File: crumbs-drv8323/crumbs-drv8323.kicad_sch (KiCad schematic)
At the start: 22 parts, among them J1 MotorConn, J2 Conn_02x05_Odd_Even, J3 Conn_02x05_Odd_Even, J4 Conn_01x02, Q1 Q_NMOS, Q2 Q_NMOS, Q3 Q_NMOS, Q4 Q_NMOS, Q5 Q_NMOS, Q6 Q_NMOS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

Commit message: feat: first iteration on drv8323 schematic
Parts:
- added C7: 100nF / 16V, Capacitor_SMD:C_0805_2012Metric, symbol Device:C
- added C8: 47uF / 16V, Capacitor_SMD:C_0805_2012Metric, symbol Device:C
- added C9: 4.7uF / VM, symbol Device:C_Polarized
- added D1: 1N5819, Diode_THT:D_DO-41_SOD81_P10.16mm_Horizontal, symbol Diode:1N5819
- added J3: VCC_to_3.3V, Connector_PinHeader_2.54mm:PinHeader_1x03_P2.54mm_Vertical, symbol Connector_Generic:Conn_01x03
- added J6: Conn_01x03, Connector_PinHeader_2.54mm:PinHeader_1x03_P2.54mm_Vertical, symbol Connector_Generic:Conn_01x03
- added L1: 22uH / 2A, symbol Device:L
- added R6: 4K7, Resistor_SMD:R_0805_2012Metric, symbol Device:R_US
- added RFBB1: 30K, Resistor_SMD:R_0805_2012Metric, symbol Device:R_US
- added RFBT1: 100K, Resistor_SMD:R_0805_2012Metric, symbol Device:R_US
- added RT1: 34K8, Resistor_SMD:R_0805_2012Metric, symbol Device:R_US
- added U2: LMR16010PDDAR, easyeda2kicad:SOPOWERPAD-8_L4.9-W3.9-P1.27-LS6.0-BL-EP, symbol easyeda2kicad:LMR16010PDDAR
- C1: renamed from C3; value C -> 22uF
- C2: value C -> 100nF
- C3: renamed from C1; value C -> 1uF/16V
- C4: value C -> 47nF
- C5: renamed from C6; value C -> 1uF/6.3V
- C6: renamed from C5; value C -> 100nF
- R1: renamed from R4; value ~ -> 4K7
- R2: renamed from R5; value ~ -> 4K7
- R3: value RSense -> 2m
- R4: renamed from R2; value RSense -> 2m
- R5: renamed from R1; value RSense -> 2m
- U1: footprint DRV8323SRTAT:QFN50P600X600X80-41N415X415 -> symbols:QFN50P600X600X80-41N415X415
- renumbered J3 to J2, J2 to J5, Q5 to Q1, Q6 to Q2, Q1 to Q5, Q2 to Q6
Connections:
- net GND: now also J5.10 (Pin_10), U1.41 (EXP), C8.1, C9.2, D1.2 (A), RFBB1.2, RT1.2, U2.7 (GND), U2.9 (EP); no longer J5.8 (Pin_8)
- net VCC: now also J3.2 (Pin_2)
- net VM: now also J5.6 (Pin_6), C9.1, U2.2 (VIN), U2.3 (EN)
- new net: RFBB1.1, RFBT1.2, U2.5 (FB)
- new net: RT1.1, U2.4 (RT/SYNC)
- new net: C7.1, U2.1 (BOOT)
- new net: C7.2, D1.1 (K), L1.1, U2.8 (SW)
- new net +3V3: C8.2, J3.1 (Pin_1), J5.8 (Pin_8), L1.2, R6.1, RFBT1.1
- new net PGOOD: R6.2, U2.6 (PGOOD)
- no-connect marks 1 -> 0
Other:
- note added: "3.3-V internal regulator output This regulator can source up to 30 mA externally"
- note added: "65V Max"
- note added: "7V to 60V"
- note added: "ALL Capacitor Must be Higher than VM"
- note added: "About 700Khz"
- note added: "R_{FBT} = ((Vout - 0.75) / 0.75) x R_{FBB} 100K = ((3.3 - 0.75) / 0.75) x R_{FBB} R_{FBB} = 29500 ohm"
- note added: "R_{T}(KOhm) = 42904 x f_{sw}(Khz) For 700 KHz, the calculated RT is 34.44 kΩ and standard value 34.8 kΩ can be used to set the switching frequency at 700 KHz"
- note added: "Thermal Pad Must be connected to ground"
- note added: "VIL Input logic low voltage 0 - 0.8 V VIH Input logic high voltage 1.5 - 5.5 V"
- note added: "VM + 13.5V"
- note added: "VREF Reference voltage input (VREF) 3 - 5.5 V"
- moved on the sheet: C1, C2, C3, C4, C5, C6, J1, J2, J4, J5, Q1, Q2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

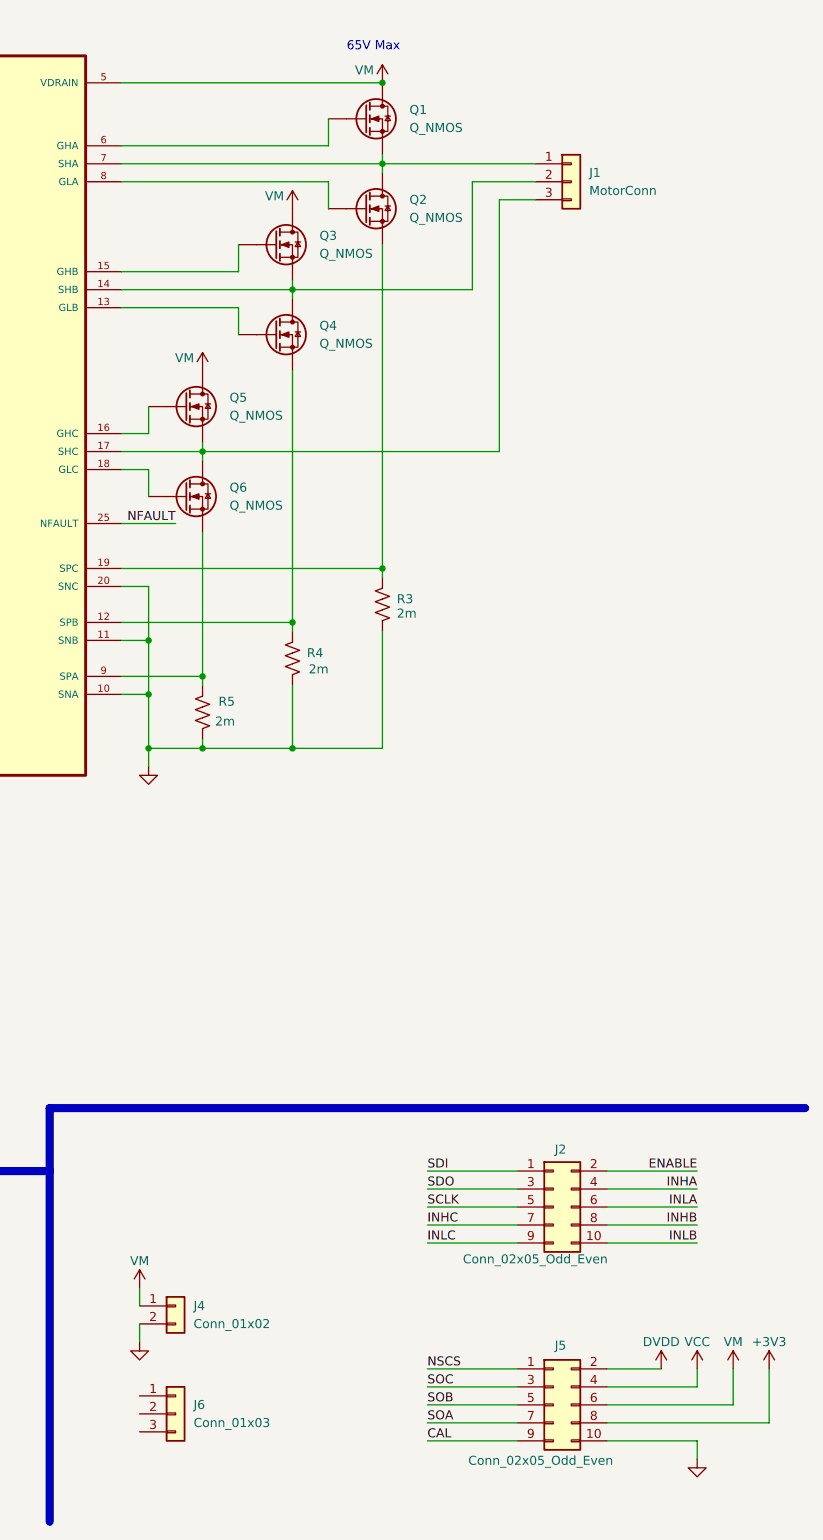
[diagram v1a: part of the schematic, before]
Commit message: feat: assign correct footprint
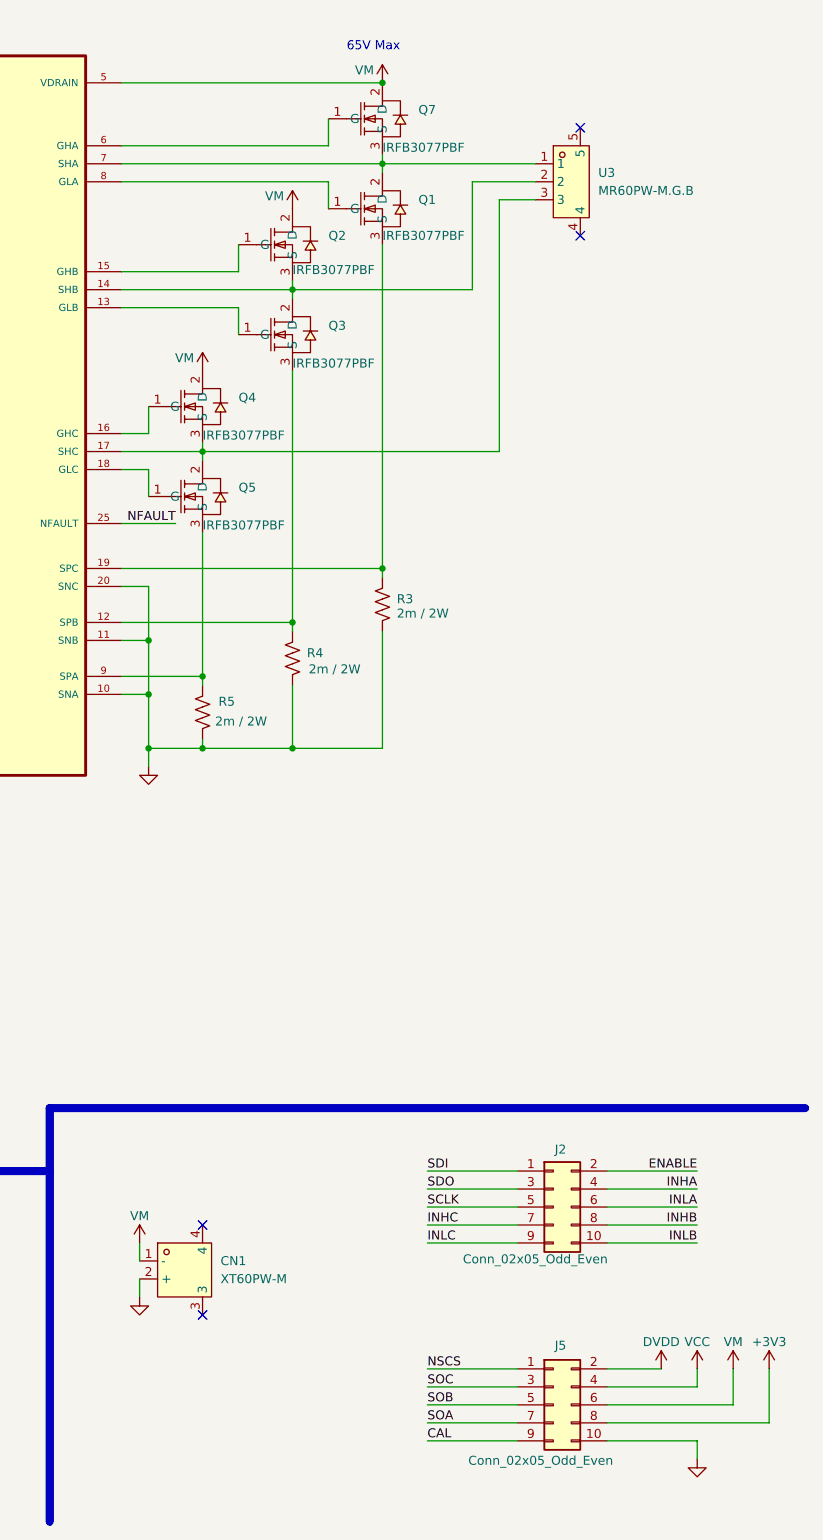
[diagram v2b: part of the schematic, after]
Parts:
- removed J1: MotorConn, symbol Connector_Generic:Conn_01x03
- removed J4: Conn_01x02, symbol Connector_Generic:Conn_01x02
- removed J6: Conn_01x03, Connector_PinHeader_2.54mm:PinHeader_1x03_P2.54mm_Vertical, symbol Connector_Generic:Conn_01x03
- removed Q1, Q2, Q3, Q4, Q5, Q6: Q_NMOS, symbol Device:Q_NMOS
- added CN1: XT60PW-M, easyeda2kicad:CONN-TH_XT60PW-M, symbol easyeda2kicad:XT60PW-M
- added Q1, Q2, Q3, Q4, Q5, Q7: IRFB3077PBF, easyeda2kicad:TO-220-3_L10.0-W4.5-P2.54-L, symbol easyeda2kicad:IRFB3077PBF
- added U3: MR60PW-M.G.B, easyeda2kicad:CONN-TH_MR60PW, symbol easyeda2kicad:MR60PW-M.G.B
- C1, C2, C4, C8: footprint Capacitor_SMD:C_0805_2012Metric -> Capacitor_THT:C_Disc_D7.5mm_W5.0mm_P5.00mm
- C9: footprint (none) -> Capacitor_THT:CP_Radial_D8.0mm_P2.50mm
- L1: footprint (none) -> Inductor_SMD:L_1812_4532Metric
- R3, R4, R5: value 2m -> 2m / 2W; footprint Resistor_SMD:R_0805_2012Metric -> Resistor_SMD:R_2512_6332Metric
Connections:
- net GND: now also CN1.2 (+)
- net VM: now also CN1.1 (-), Q2.2 (D), Q4.2 (D), Q7.2 (D)
- net at R4.1, U1.12 (SPB): now also Q3.3 (S)
- net at U1.13 (GLB): now also Q3.1 (G)
- net at U1.14 (SHB): now also Q2.3 (S), Q3.2 (D), U3.2
- net at U1.15 (GHB): now also Q2.1 (G)
- net at U1.16 (GHC): now also Q4.1 (G)
- net at U1.17 (SHC): now also Q4.3 (S), Q5.2 (D), U3.3
- net at U1.18 (GLC): now also Q5.1 (G)
- net at R3.1, U1.19 (SPC): now also Q1.3 (S)
- net at U1.6 (GHA): now also Q7.1 (G)
- net at U1.7 (SHA): now also Q1.2 (D), Q7.3 (S), U3.1
- net at U1.8 (GLA): now also Q1.1 (G)
- net at R5.1, U1.9 (SPA): now also Q5.3 (S)
- no-connect marks 0 -> 4

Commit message: feat: drv8323 finish routing
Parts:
- added H1, H2, H3, H4: MountingHole, MountingHole:MountingHole_2mm, symbol Mechanical:MountingHole
- Q1, Q2, Q3, Q4, Q5, Q7: footprint easyeda2kicad:TO-220-3_L10.0-W4.5-P2.54-L -> Package_TO_SOT_THT:TO-220-3_Horizontal_TabDown
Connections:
- net +3V3: now also J5.4 (Pin_4); no longer J5.8 (Pin_8)
- net CAL: now also J2.2 (Pin_2); no longer J5.9 (Pin_9)
- net ENABLE: now also J2.4 (Pin_4); no longer J2.2 (Pin_2)
- net GND: now also J5.3 (Pin_3); no longer J5.10 (Pin_10)
- net INHA: now also J5.1 (Pin_1); no longer J2.4 (Pin_4)
- net INHB: now also J5.7 (Pin_7); no longer J2.8 (Pin_8)
- net INHC: now also J5.10 (Pin_10); no longer J2.7 (Pin_7)
- net INLA: now also J5.5 (Pin_5); no longer J2.6 (Pin_6)
- net INLB: now also J5.9 (Pin_9); no longer J2.10 (Pin_10)
- net INLC: now also J5.8 (Pin_8); no longer J2.9 (Pin_9)
- net NSCS: now also J2.6 (Pin_6); no longer J5.1 (Pin_1)
- net SCLK: now also J2.8 (Pin_8); no longer J2.5 (Pin_5)
- net SDI: now also J2.10 (Pin_10); no longer J2.1 (Pin_1)
- net SDO: now also J2.9 (Pin_9); no longer J2.3 (Pin_3)
- net SOA: now also J2.5 (Pin_5); no longer J5.7 (Pin_7)
- net SOB: now also J2.3 (Pin_3); no longer J5.5 (Pin_5)
- net SOC: now also J2.1 (Pin_1); no longer J5.3 (Pin_3)
- net VCC: now also J2.7 (Pin_7); no longer J5.4 (Pin_4)
- net spb: now reaches Q3.3 (S), R4.1, U1.12 (SPB)
- net gla: now reaches Q1.1 (G), U1.8 (GLA)
- net sha: now reaches Q1.2 (D), Q7.3 (S), U1.7 (SHA), U3.1
- net spc: now reaches Q1.3 (S), R3.1, U1.19 (SPC)
- net cpl: now reaches C4.2, U1.1 (CPL)
- net glb: now reaches Q3.1 (G), U1.13 (GLB)
- net shb: now reaches Q2.3 (S), Q3.2 (D), U1.14 (SHB), U3.2
- net ghb: now reaches Q2.1 (G), U1.15 (GHB)
- net ghc: now reaches Q4.1 (G), U1.16 (GHC)
- net shc: now reaches Q4.3 (S), Q5.2 (D), U1.17 (SHC), U3.3
- net glc: now reaches Q5.1 (G), U1.18 (GLC)
- net cph: now reaches C4.1, U1.2 (CPH)
- net gha: now reaches Q7.1 (G), U1.6 (GHA)
- net spa: now reaches Q5.3 (S), R5.1, U1.9 (SPA)
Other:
- moved on the sheet: CN1, J2, J5
